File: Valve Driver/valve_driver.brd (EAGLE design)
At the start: 80 x 80 mm, 15 parts

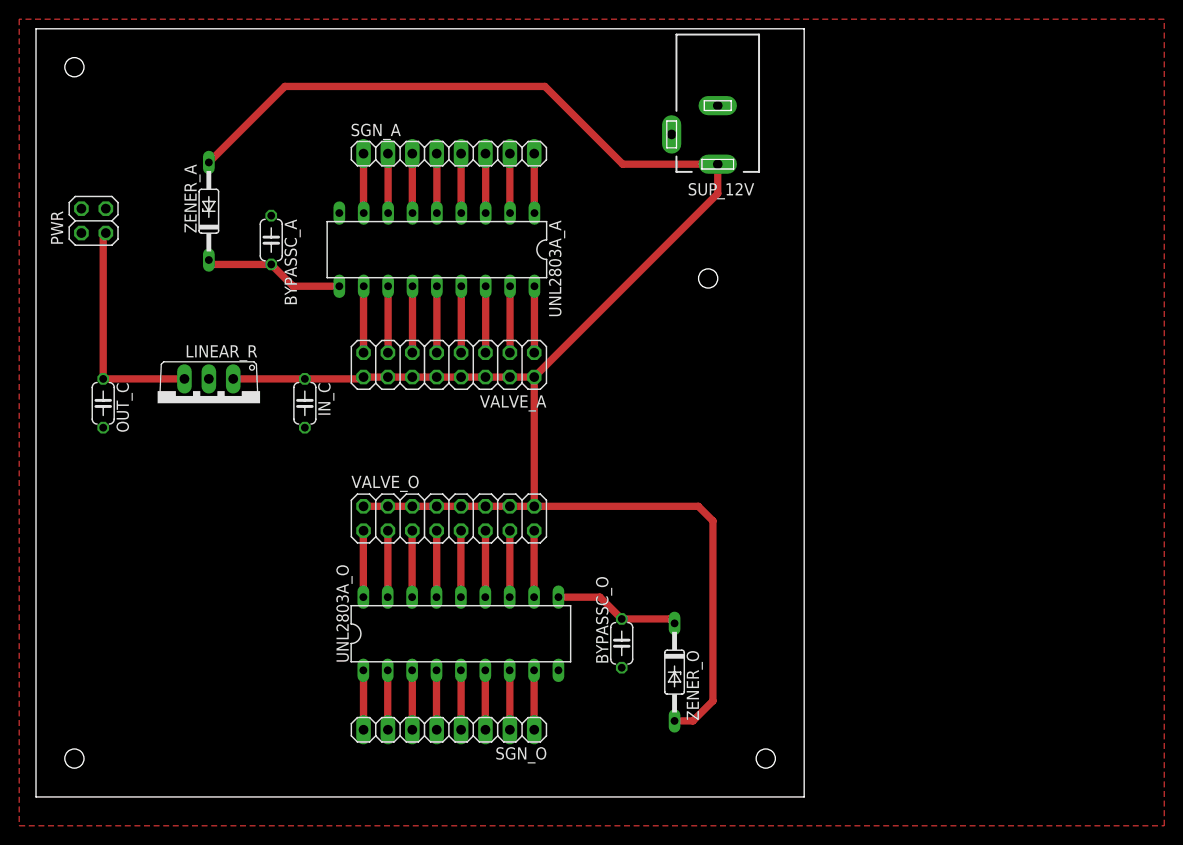
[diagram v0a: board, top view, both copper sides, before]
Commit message: 20180719-Fix-problem-for-LVB
1. OSC part: left top 6th channel cannot be arranged, change pin to left top 5th

2.change the area of HVB
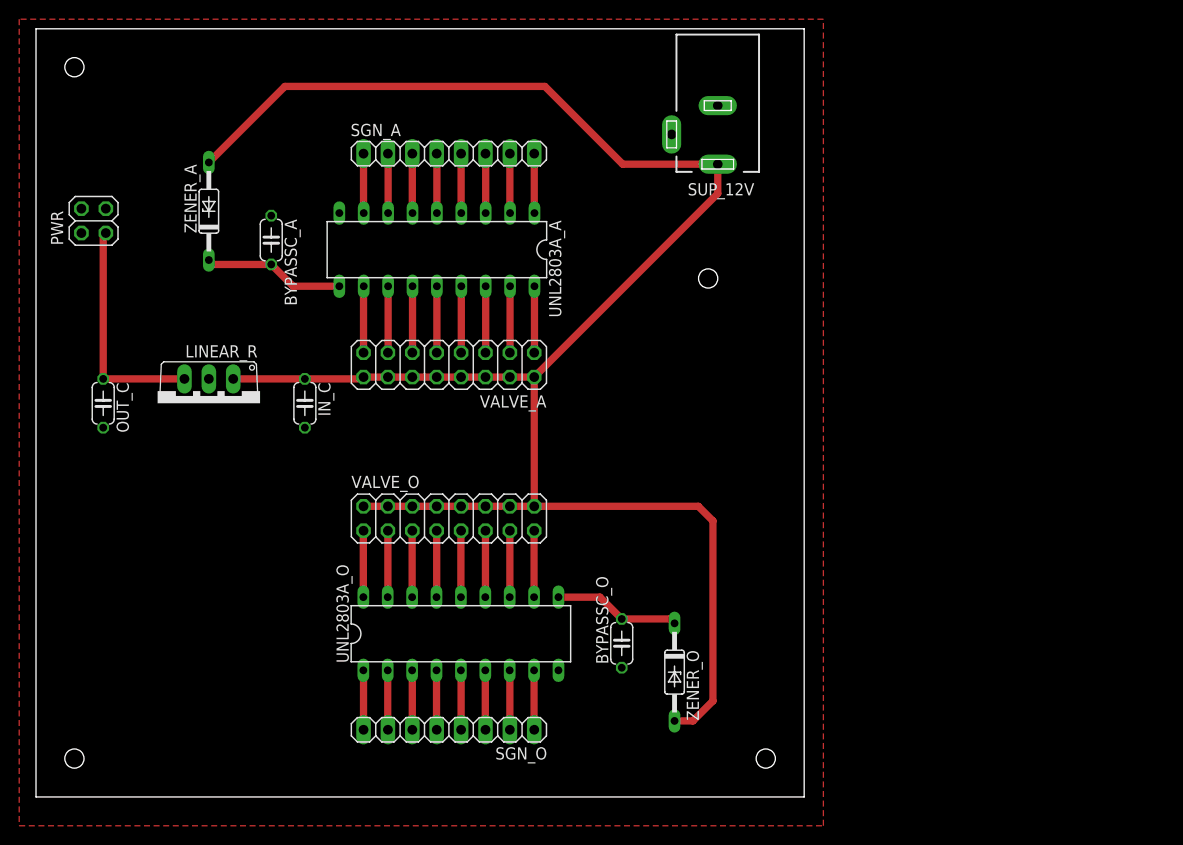
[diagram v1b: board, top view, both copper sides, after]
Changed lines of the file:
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@@
 <vertex x="-1.75" y="81"/>
 <vertex x="-1.75" y="-3"/>
-<vertex x="117.5" y="-3"/>
-<vertex x="117.5" y="81"/>
+<vertex x="82" y="-3"/>
+<vertex x="82" y="81"/>
 </polygon>
 </signal>
